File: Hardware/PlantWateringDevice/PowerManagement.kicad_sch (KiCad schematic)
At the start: 23 parts, among them J6 Barrel_Jack_Switch, M1 Motor_DC, Q1 AO3404A, U2 L78L33_SO8

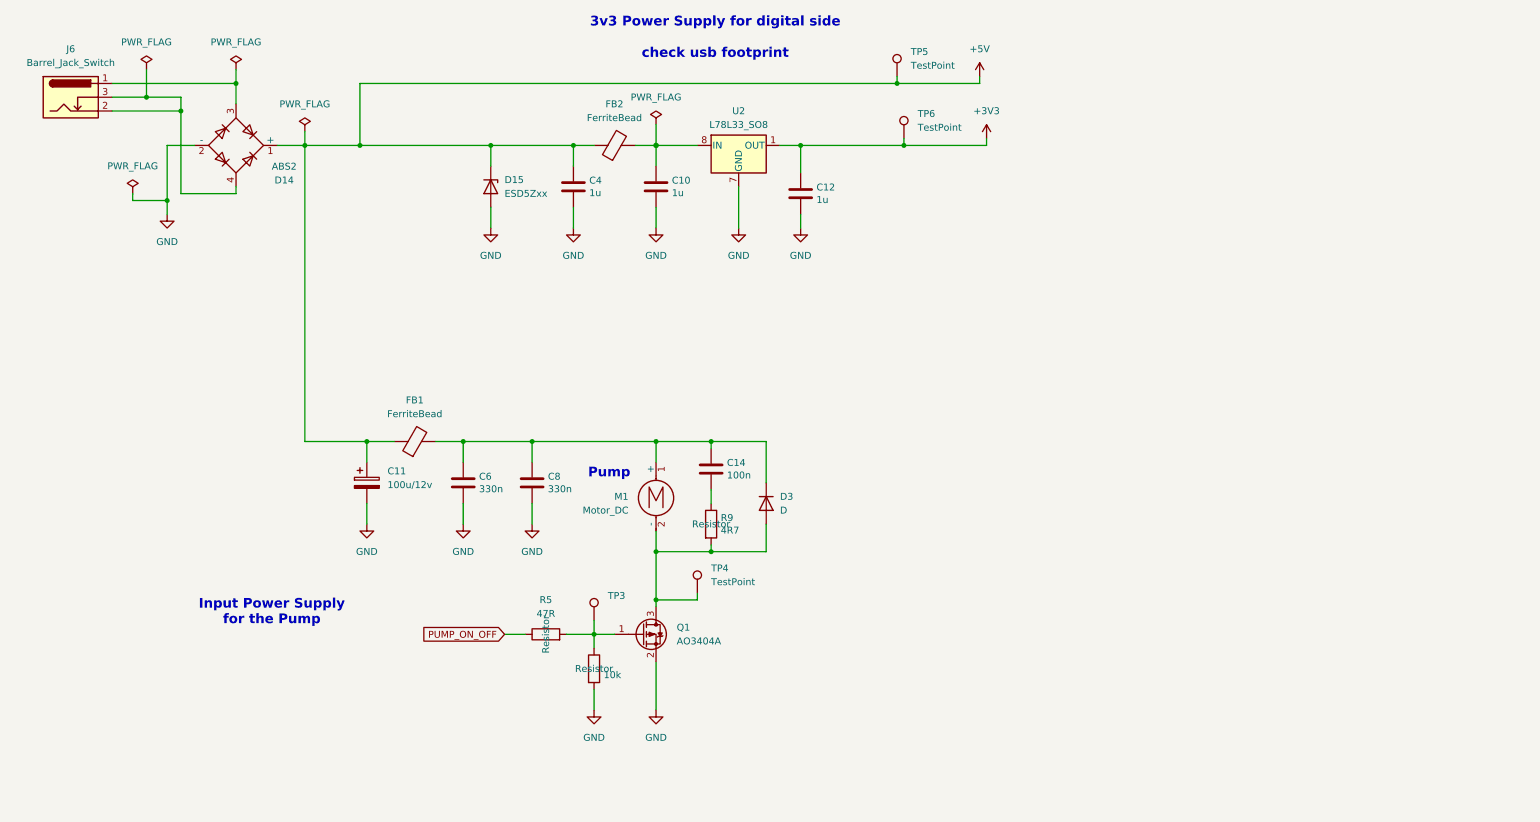
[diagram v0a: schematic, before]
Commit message: circuit simplification
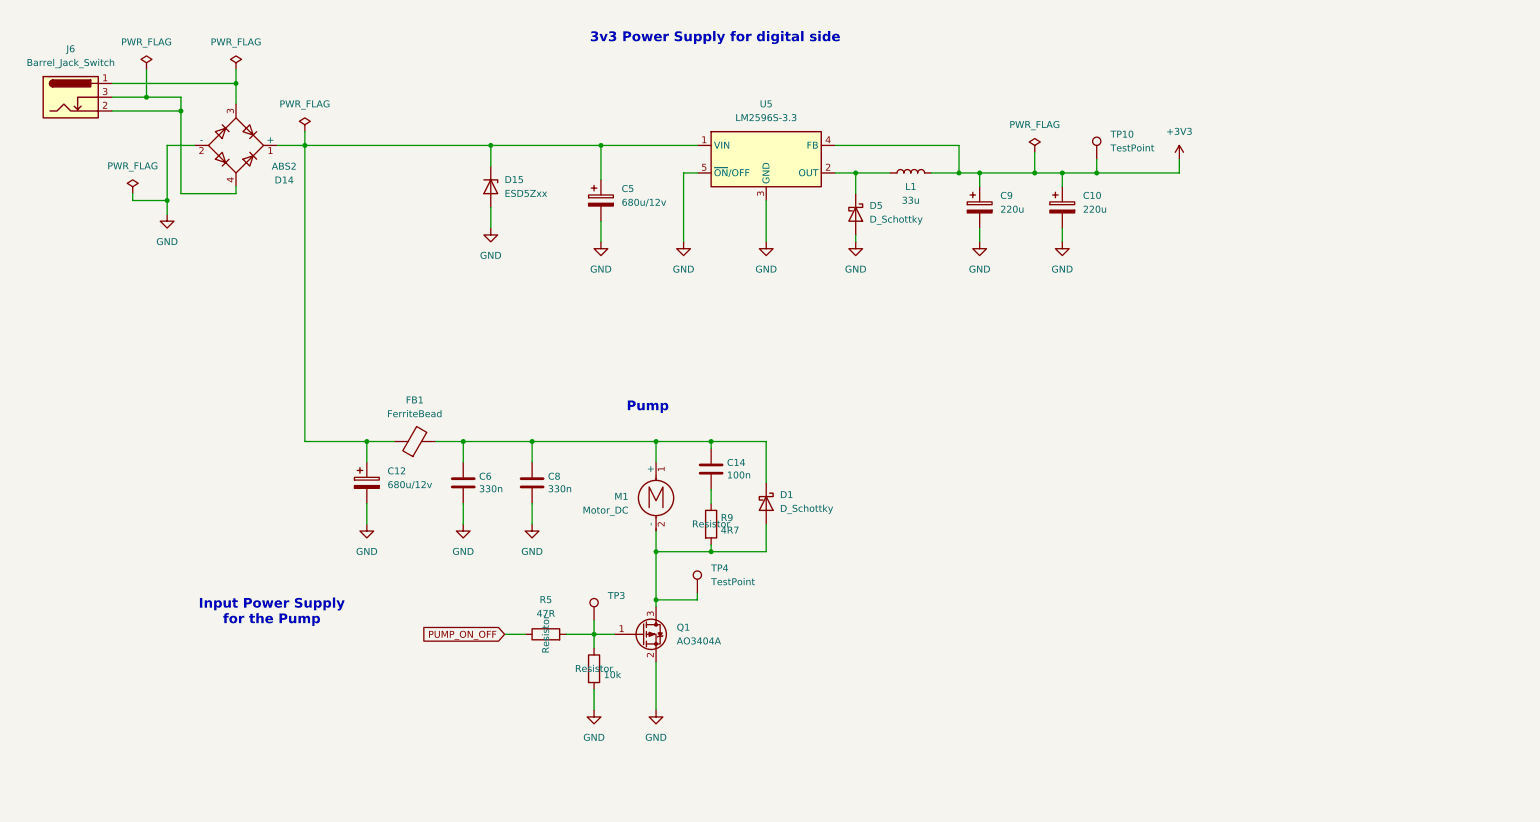
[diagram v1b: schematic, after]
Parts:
- removed C10, C12, C4: 1u, Capacitor_SMD:C_0805_2012Metric, symbol Device:C
- removed C11: 100u/12v, Capacitor_SMD:CP_Elec_6.3x5.8, symbol Device:C_Polarized
- removed D3: D, Diode_SMD:D_MiniMELF, symbol Device:D
- removed FB2: FerriteBead, Inductor_SMD:L_0805_2012Metric_Pad1.15x1.40mm_HandSolder, symbol Device:FerriteBead
- removed TP5, TP6: TestPoint, TestPoint:TestPoint_Pad_D2.0mm, symbol Connector:TestPoint
- removed U2: L78L33_SO8, Package_SO:SOIC-8_3.9x4.9mm_P1.27mm, symbol Regulator_Linear:L78L33_SO8
- added C10, C9: 220u, Capacitor_SMD:CP_Elec_6.3x5.8, symbol Device:C_Polarized
- added C12, C5: 680u/12v, Capacitor_SMD:CP_Elec_10x10, symbol Device:C_Polarized
- added D1, D5: D_Schottky, Diode_SMD:D_SMA, symbol Device:D_Schottky
- added L1: 33u, PlantWateringDevice:SDR1006-330KL, symbol Device:L
- added TP10: TestPoint, TestPoint:TestPoint_Pad_D1.5mm, symbol Connector:TestPoint
- added U5: LM2596S-3.3, Package_SO:Infineon_PG-DSO-8-27_3.9x4.9mm_EP2.65x3mm, symbol Regulator_Switching:LM2596S-3.3
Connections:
- net +3V3: now also C10.1, C9.1, L1.2, TP10.1, U5.4 (FB)
- net GND: now also C10.2, C12.2, C5.2, C9.2, D5.2 (A), U5.3 (GND), U5.5 (~{ON}/OFF)
- net at M1.2 (-), Q1.3 (D), R9.2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: now also D1.2 (A)
- net at C14.1, C6.1, C8.1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: now also D1.1 (K)
- net +5V: no longer names the net of D14.1 (+), D15.1 (K), FB1.1
- net +5V: now also C12.1, C5.1, U5.1 (VIN)
- new net: D5.1 (K), L1.1, U5.2 (OUT)
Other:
- note added: "3v3 Power Supply for digital side"
- note removed: "3v3 Power Supply for digital side check usb footprint"

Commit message: improvements after eric's comments
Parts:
- removed C10, C9: 220u, Capacitor_SMD:CP_Elec_6.3x5.8, symbol Device:C_Polarized
- removed D1, D5: D_Schottky, Diode_SMD:D_SMA, symbol Device:D_Schottky
- removed D15: ESD5Zxx, Diode_SMD:D_SOD-523, symbol Diode:ESD5Zxx
- removed FB1: FerriteBead, Inductor_SMD:L_0805_2012Metric_Pad1.15x1.40mm_HandSolder, symbol Device:FerriteBead
- removed L1: 33u, PlantWateringDevice:SDR1006-330KL, symbol Device:L
- removed U5: LM2596S-3.3, Package_SO:Infineon_PG-DSO-8-27_3.9x4.9mm_EP2.65x3mm, symbol Regulator_Switching:LM2596S-3.3
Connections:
- net +3V3 is gone; now on net VCC: TP10.1
- net VCC: now reaches C12.1, C5.1, D14.1 (+)
- net VCC: now also C14.1, C6.1, C8.1, M1.1 (+)
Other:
- note added: "Power Supply for digital side"
- note removed: "3v3 Power Supply for digital side"
- moved on the sheet: C5, TP10

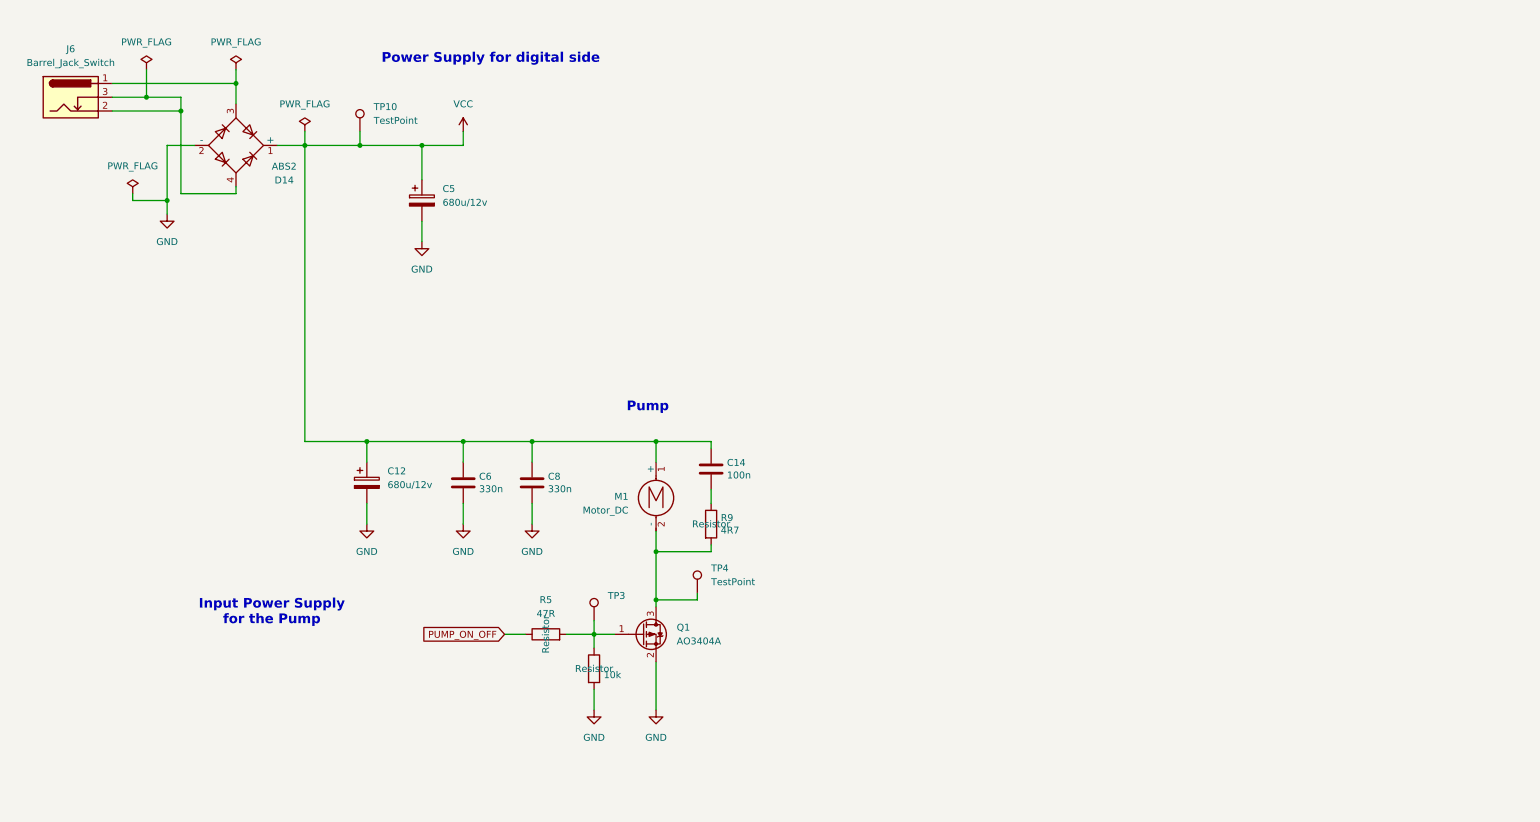
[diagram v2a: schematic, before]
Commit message: fixes before sending pcb and 3d model to production
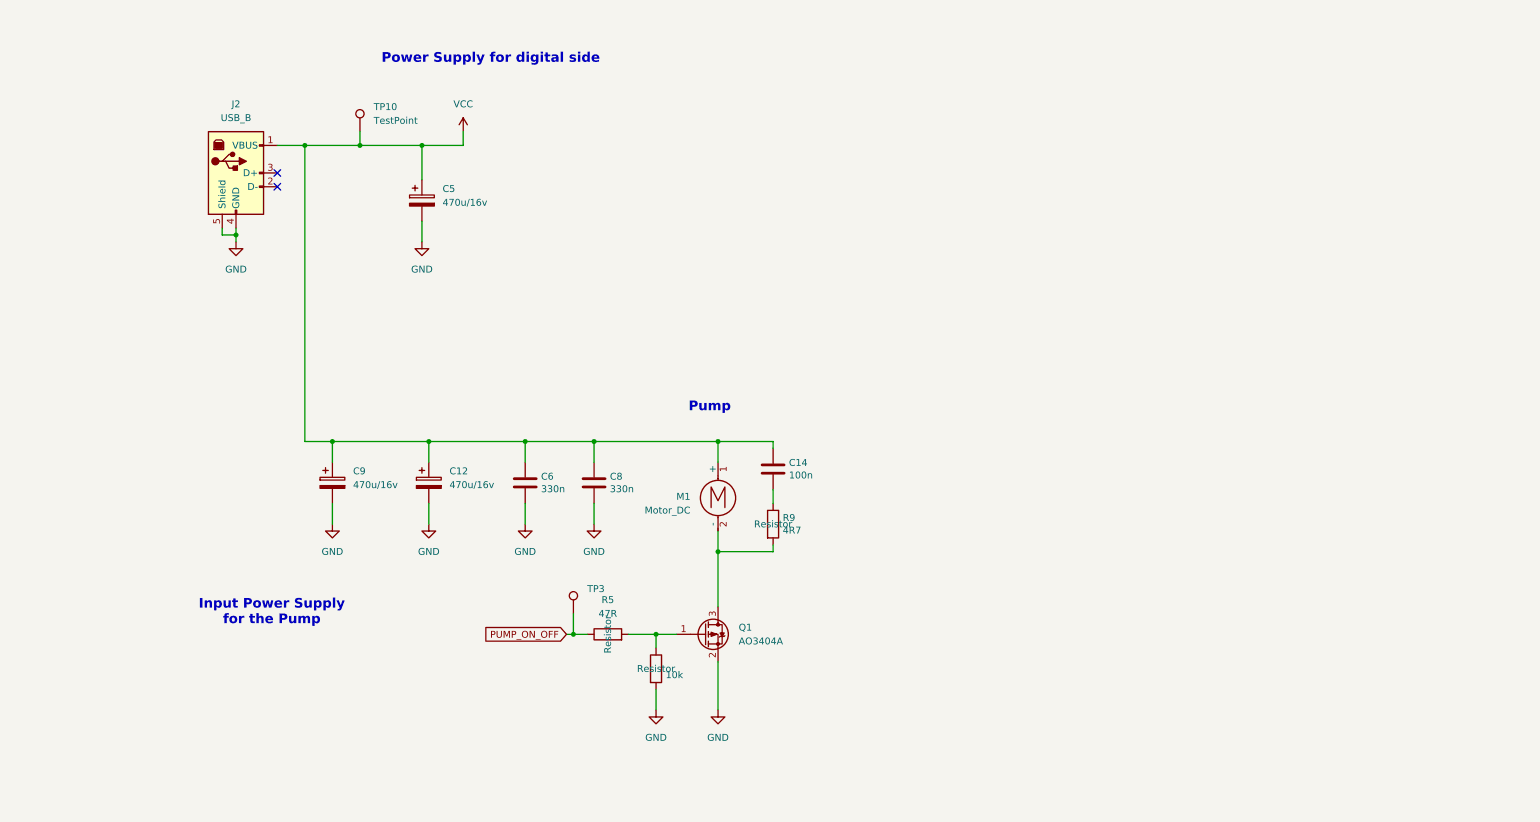
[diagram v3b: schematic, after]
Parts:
- removed D14: ABS2, Diode_SMD:Diode_Bridge_Diotec_ABS, symbol Diode_Bridge:ABS2
- removed J6: Barrel_Jack_Switch, Connector_BarrelJack:BarrelJack_GCT_DCJ200-10-A_Horizontal, symbol Connector:Barrel_Jack_Switch
- removed TP4: TestPoint, TestPoint:TestPoint_Pad_D2.0mm, symbol Connector:TestPoint
- added C9: 470u/16v, Capacitor_SMD:CP_Elec_8x10, symbol Device:C_Polarized
- added J2: USB_B, Connector_USB:USB_B_OST_USB-B1HSxx_Horizontal, symbol Connector:USB_B
- C12, C5: value 680u/12v -> 470u/16v; footprint Capacitor_SMD:CP_Elec_10x10 -> Capacitor_SMD:CP_Elec_8x10
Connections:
- net GND: now also C9.2, J2.4 (GND), J2.5 (Shield)
- net PUMP_ON_OFF: now also TP3.1
- net VCC: now also C9.1, J2.1 (VBUS)
- net at Q1.1 (G), R5.2, R7.1: no longer TP3.1
- no-connect marks 0 -> 2
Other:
- moved on the sheet: C12, C14, C6, C8, M1, Q1, R5, R9, TP3

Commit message: firmware implementation
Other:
- note added: "CHANGE TRANSITOR TYPE AND COMPONENT PART"
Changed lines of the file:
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@@
+		)
+	)
+	(text "CHANGE TRANSITOR TYPE AND COMPONENT PART\n"
+		(exclude_from_sim no)
+		(at 197.612 170.942 0)
+		(effects
+			(font
+				(size 5.08 5.08)
+				(thickness 1.27)
+				(bold yes)
+			)
 		)
 	)

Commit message: fix #29, fix #31
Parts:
- removed Q1: AO3404A, Package_TO_SOT_SMD:SOT-23, symbol Transistor_FET:AO3401A
- added Q1: AO3404A, Package_TO_SOT_SMD:SOT-23, symbol Transistor_FET:AO3400A
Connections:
- net GND: now also Q1.2 (S)
- net at R5.2, R7.1: now also Q1.1 (G)
- net at M1.2 (-), R9.2: now also Q1.3 (D)
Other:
- note removed: "CHANGE TRANSITOR TYPE AND COMPONENT PART"
- note removed: "Pump"
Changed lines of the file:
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@@
-		)
-	)
-	(text "Pump"
-		(exclude_from_sim no)
-		(at 157.226 101.6 0)
-		(effects
-			(font
-				(size 1.778 1.778)
-				(thickness 0.4064)
-				(bold yes)
-			)
-		)
-	)
-	(text "CHANGE TRANSITOR TYPE AND COMPONENT PART\n"
-		(exclude_from_sim no)
-		(at 197.612 170.942 0)
-		(effects
-			(font
-				(size 5.08 5.08)
-				(thickness 1.27)
-				(bold yes)
-			)
 		)
 	)
@@
 	)
 	(symbol
-		(lib_id "Device:C")
-		(at 123.19 115.57 0)
-		(unit 1)
-		(exclude_from_sim no)
-		(in_bom yes)
-		(on_board yes)
-		(dnp no)
-		(property "Reference" "C6"
-			(at 126.111 114.4016 0)
-			(effects
-				(font
-					(size 1.27 1.27)
-				)
-				(justify left)
-			)
-		)
-		(property "Value" "330n"
-			(at 126.111 116.713 0)
-			(effects
-				(font
-					(size 1.27 1.27)
-				)
-				(justify left)
-			)
-		)
-		(property "Footprint" "Capacitor_SMD:C_0805_2012Metric"
-			(at 124.1552 119.38 0)
-			(effects
-				(font
-					(size 1.27 1.27)
-				)
-				(hide yes)
-			)
-		)
-		(property "Datasheet" "~"
-			(at 123.19 115.57 0)
-			(effects
-				(font
-					(size 1.27 1.27)
-				)
-				(hide yes)
-			)
-		)
-		(property "Description" "Unpolarized capacitor"
-			(at 123.19 115.57 0)
-			(effects
-				(font
-					(size 1.27 1.27)
-				)
-				(hide yes)
-			)
-		)
-		(pin "1"
-		)
-		(pin "2"
-		)
-		(instances
-			(project "PlantWateringDevice"
-				(path "/1ef241b3-83d7-48ae-bcca-b7d0eea44e63/0c2157b4-5762-411a-834e-73665a569667"
-					(reference "C6")
-					(unit 1)
-				)
-			)
-		)
-	)
-	(symbol
-		(lib_id "Transistor_FET:AO3401A")
+		(lib_id "Transistor_FET:AO3400A")
 		(at 156.21 143.51 0)
 		(unit 1)
@@
 			)
 		)
-		(property "Datasheet" "http://www.aosmd.com/pdfs/datasheet/AO3401A.pdf"
+		(property "Datasheet" "http://www.aosmd.com/pdfs/datasheet/AO3400A.pdf"
 			(at 161.29 147.32 0)
 			(effects
@@
 			)
 		)
-		(property "Description" "-4.0A Id, -30V Vds, P-Channel MOSFET, SOT-23"
+		(property "Description" "30V Vds, 5.7A Id, N-Channel MOSFET, SOT-23"
 			(at 156.21 143.51 0)
 			(effects
@@
 			)
 		)
-		(pin "1"
-		)
 		(pin "3"
 		)
+		(pin "1"
+		)
 		(pin "2"
 		)
@@
 					(unit 1)
 				)
+			)
+		)
+	)
+	(symbol
+		(lib_id "Device:C")
+		(at 123.19 115.57 0)
+		(unit 1)
+		(exclude_from_sim no)
+		(in_bom yes)
+		(on_board yes)
+		(dnp no)
+		(property "Reference" "C6"
+			(at 126.111 114.4016 0)
+			(effects
+				(font
+					(size 1.27 1.27)
+				)
+				(justify left)
+			)
+		)
+		(property "Value" "330n"
+			(at 126.111 116.713 0)
+			(effects
+				(font
+					(size 1.27 1.27)
+				)
+				(justify left)
+			)
+		)
+		(property "Footprint" "Capacitor_SMD:C_0805_2012Metric"
+			(at 124.1552 119.38 0)
+			(effects
+				(font
+					(size 1.27 1.27)
+				)
+				(hide yes)
+			)
+		)
+		(property "Datasheet" "~"
+			(at 123.19 115.57 0)
+			(effects
+				(font
+					(size 1.27 1.27)
+				)
+				(hide yes)
+			)
+		)
+		(property "Description" "Unpolarized capacitor"
+			(at 123.19 115.57 0)
+			(effects
+				(font
+					(size 1.27 1.27)
+				)
+				(hide yes)
+			)
+		)
+		(pin "1"
+		)
+		(pin "2"
+		)
+		(instances
+			(project "PlantWateringDevice"
+				(path "/1ef241b3-83d7-48ae-bcca-b7d0eea44e63/0c2157b4-5762-411a-834e-73665a569667"
+					(reference "C6")
+					(unit 1)
+				)
